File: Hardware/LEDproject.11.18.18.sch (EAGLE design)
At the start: 14 parts, among them IC1 ATMEGA328-PU, Y1 16MHz

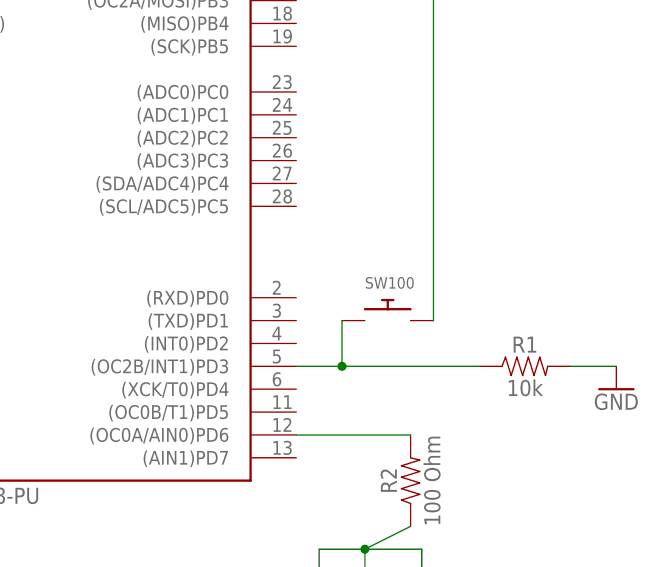
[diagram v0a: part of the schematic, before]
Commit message: Adjusted PCB mounting hole, preliminary mechanical drawings
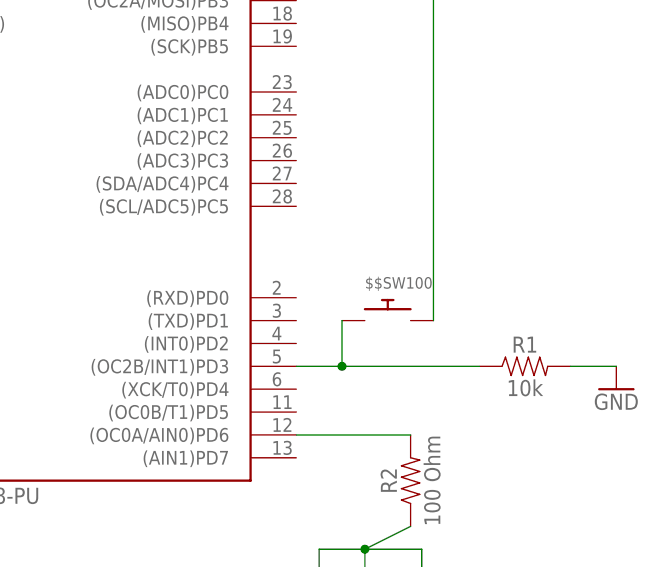
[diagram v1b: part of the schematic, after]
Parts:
- renumbered SW100 to $$SW100
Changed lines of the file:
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@@
 <part name="GND1" library="SparkFun-PowerSymbols" library_urn="urn:adsk.eagle:library:530" deviceset="GND" device=""/>
 <part name="GND4" library="SparkFun-PowerSymbols" library_urn="urn:adsk.eagle:library:530" deviceset="GND" device=""/>
-<part name="SW100" library="adafruit" library_urn="urn:adsk.eagle:library:420" deviceset="SWITCH_PUSHBUTTON" device="EVQ-PE" package3d_urn="urn:adsk.eagle:package:6240957/1"/>
+<part name="$$SW100" library="adafruit" library_urn="urn:adsk.eagle:library:420" deviceset="SWITCH_PUSHBUTTON" device="EVQ-PE" package3d_urn="urn:adsk.eagle:package:6240957/1"/>
 <part name="S100" library="adafruit" library_urn="urn:adsk.eagle:library:420" deviceset="EG1218" device="S" package3d_urn="urn:adsk.eagle:package:6240649/1"/>
 <part name="C1" library="adafruit" library_urn="urn:adsk.eagle:library:420" deviceset="C-US" device="025-030X050" package3d_urn="urn:adsk.eagle:package:6240322/1">
@@
 <attribute name="VALUE" x="17.78" y="73.406" size="1.778" layer="96" align="top-center"/>
 </instance>
-<instance part="SW100" gate="G$1" x="101.6" y="22.86">
+<instance part="$$SW100" gate="G$1" x="101.6" y="22.86">
 <attribute name="NAME" x="99.06" y="26.416" size="1.27" layer="95"/>
 <attribute name="VALUE" x="99.06" y="20.574" size="1.27" layer="96"/>
@@
 <segment>
 <pinref part="IC1" gate="IC" pin="(OC2B/INT1)PD3"/>
-<pinref part="SW100" gate="G$1" pin="P$1"/>
+<pinref part="$$SW100" gate="G$1" pin="P$1"/>
 <wire x1="91.44" y1="17.78" x2="96.52" y2="17.78" width="0.1524" layer="91"/>
 <wire x1="96.52" y1="17.78" x2="96.52" y2="22.86" width="0.1524" layer="91"/>
@@
 </segment>
 <segment>
-<pinref part="SW100" gate="G$1" pin="P$2"/>
+<pinref part="$$SW100" gate="G$1" pin="P$2"/>
 <wire x1="35.56" y1="83.82" x2="40.64" y2="83.82" width="0.1524" layer="91"/>
 <wire x1="40.64" y1="83.82" x2="106.68" y2="83.82" width="0.1524" layer="91"/>
